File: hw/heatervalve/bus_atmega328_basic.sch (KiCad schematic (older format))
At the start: 26 parts, among them J3 CONN-ISP-6, J4 WAGO 243-723, J5 WAGO 243-724, J6 WAGO 243-721, J7 WAGO 243-722, U1 25LC256, U2 ATMEGA328-TQFP32, U3 7,3728MHz, U4 MAX487ECSA, U5 AM1S-2405

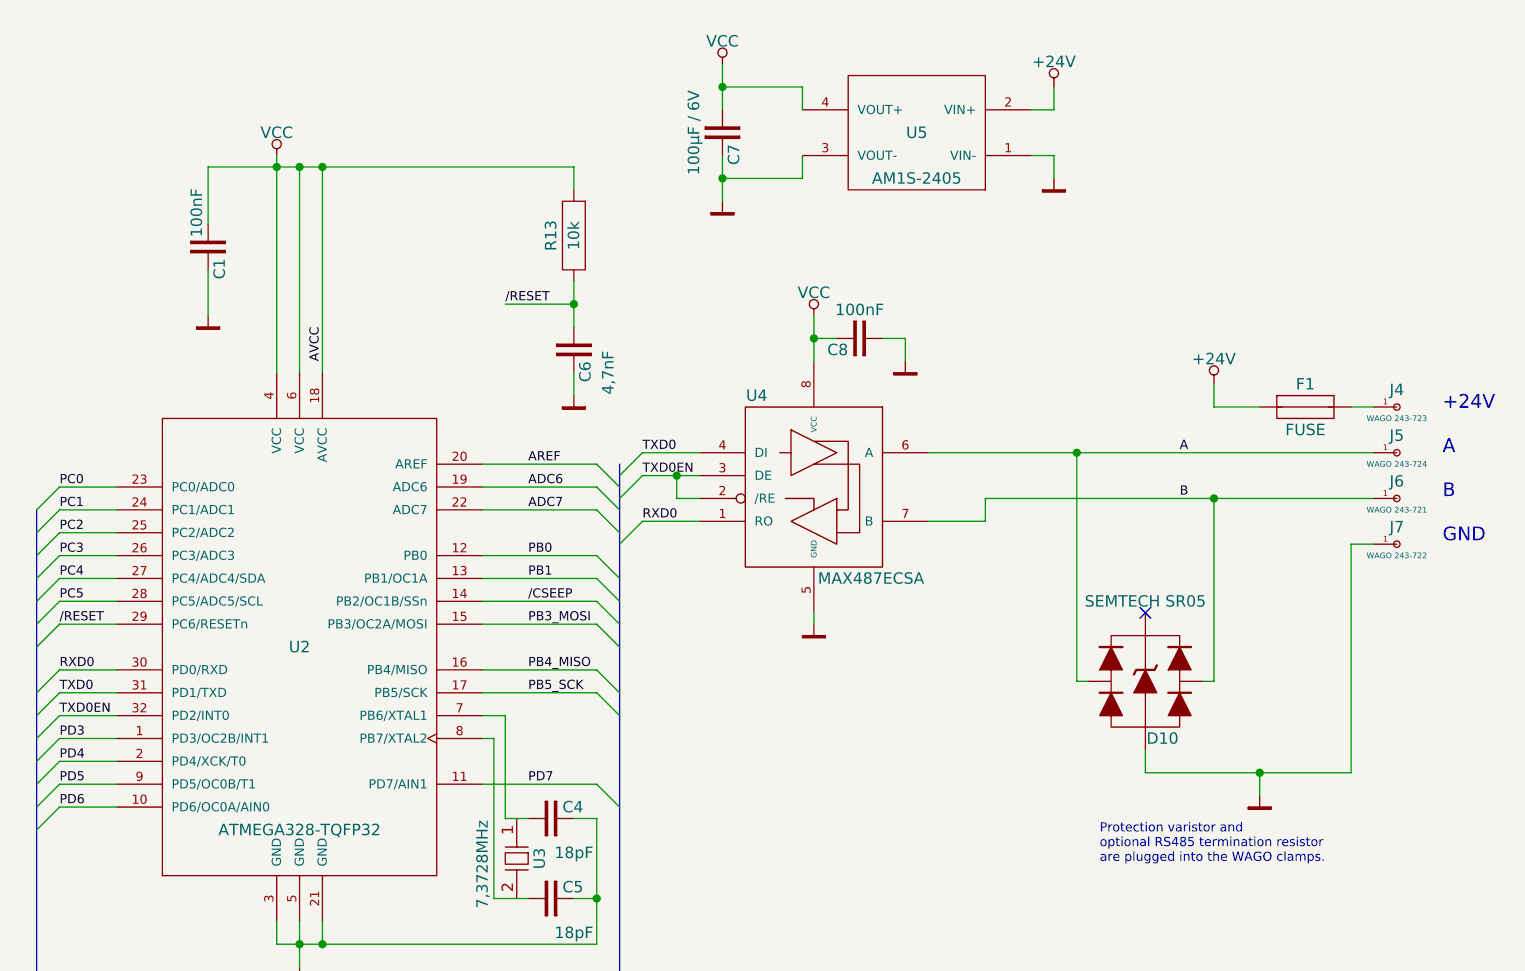
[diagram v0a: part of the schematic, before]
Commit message: first complete draft of heatervalve schematic
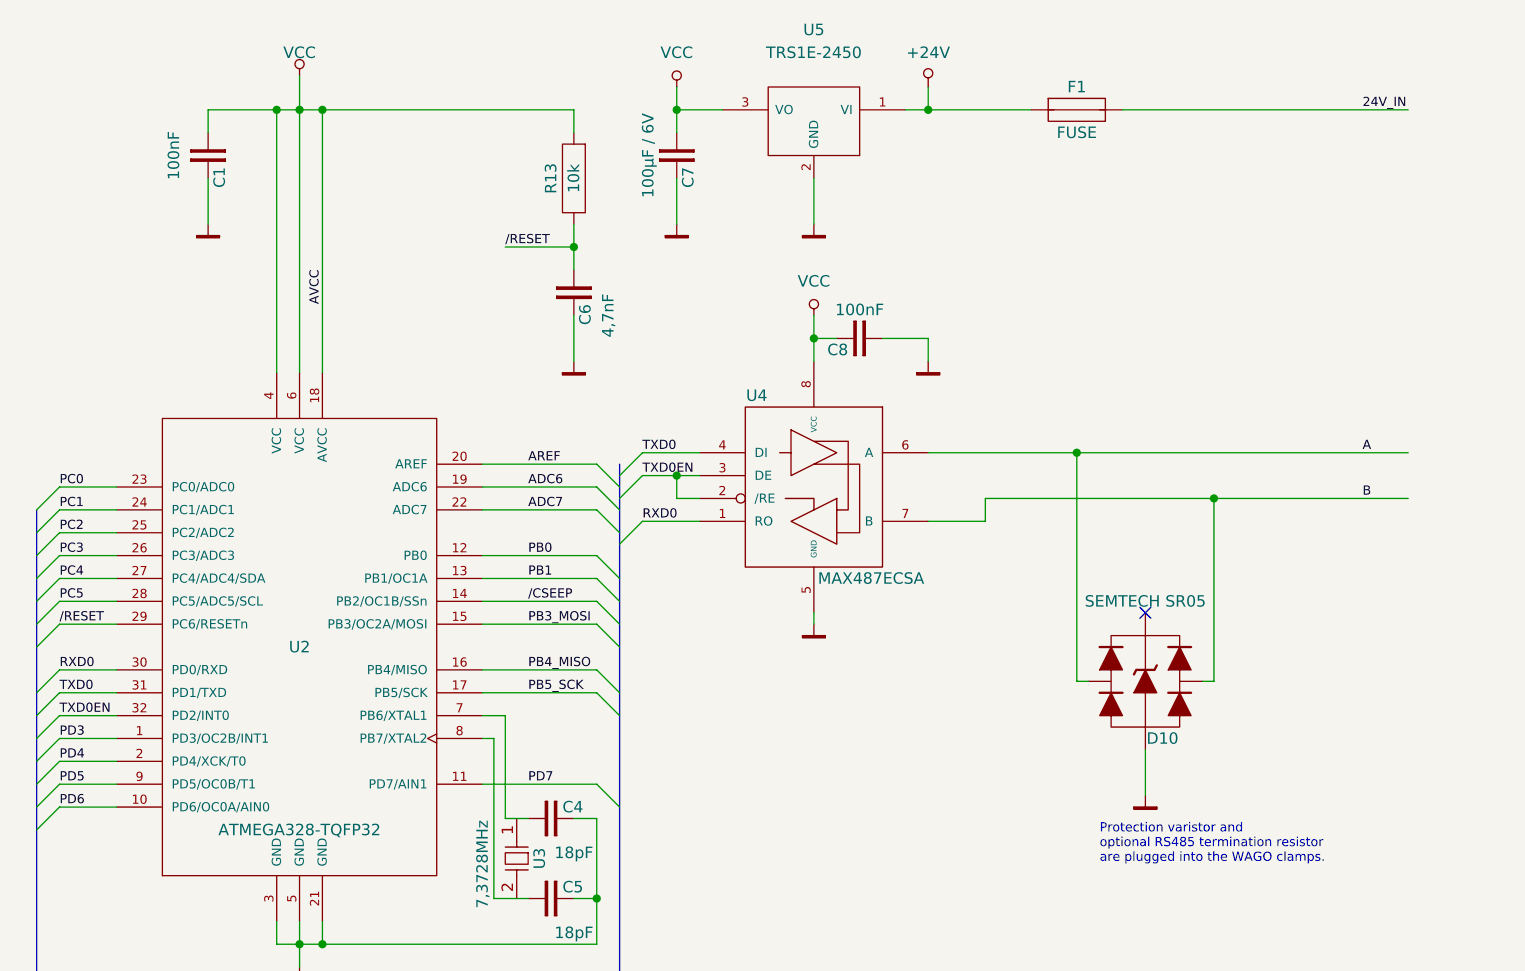
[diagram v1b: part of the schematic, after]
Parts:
- removed J4: WAGO 243-723, Connector_WAGO:WAGO_243, symbol connectors:CONN_1
- removed J5: WAGO 243-724, Connector_WAGO:WAGO_243, symbol connectors:CONN_1
- removed J6: WAGO 243-721, Connector_WAGO:WAGO_243, symbol connectors:CONN_1
- removed J7: WAGO 243-722, Connector_WAGO:WAGO_243, symbol connectors:CONN_1
- removed U5: AM1S-2405, DCDC_Converter:AM1S-XXXX_SIL4, symbol ics_regulator:AM1S-2405
- added U5: TRS1E-2450, DCDC_Converter:TRS1E_SIL3, symbol ics_regulator:TRS1E-2450
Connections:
- net +24V: now also U5.1 (VI)
- net GND: now also U5.2 (GND)
- net VCC: now also U5.3 (VO)
- net 24V_IN: now reaches F1.2
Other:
- note removed: "+24V\n\nA\n\nB \n\nGND"
- moved on the sheet: C1, C6, C7, F1, R13

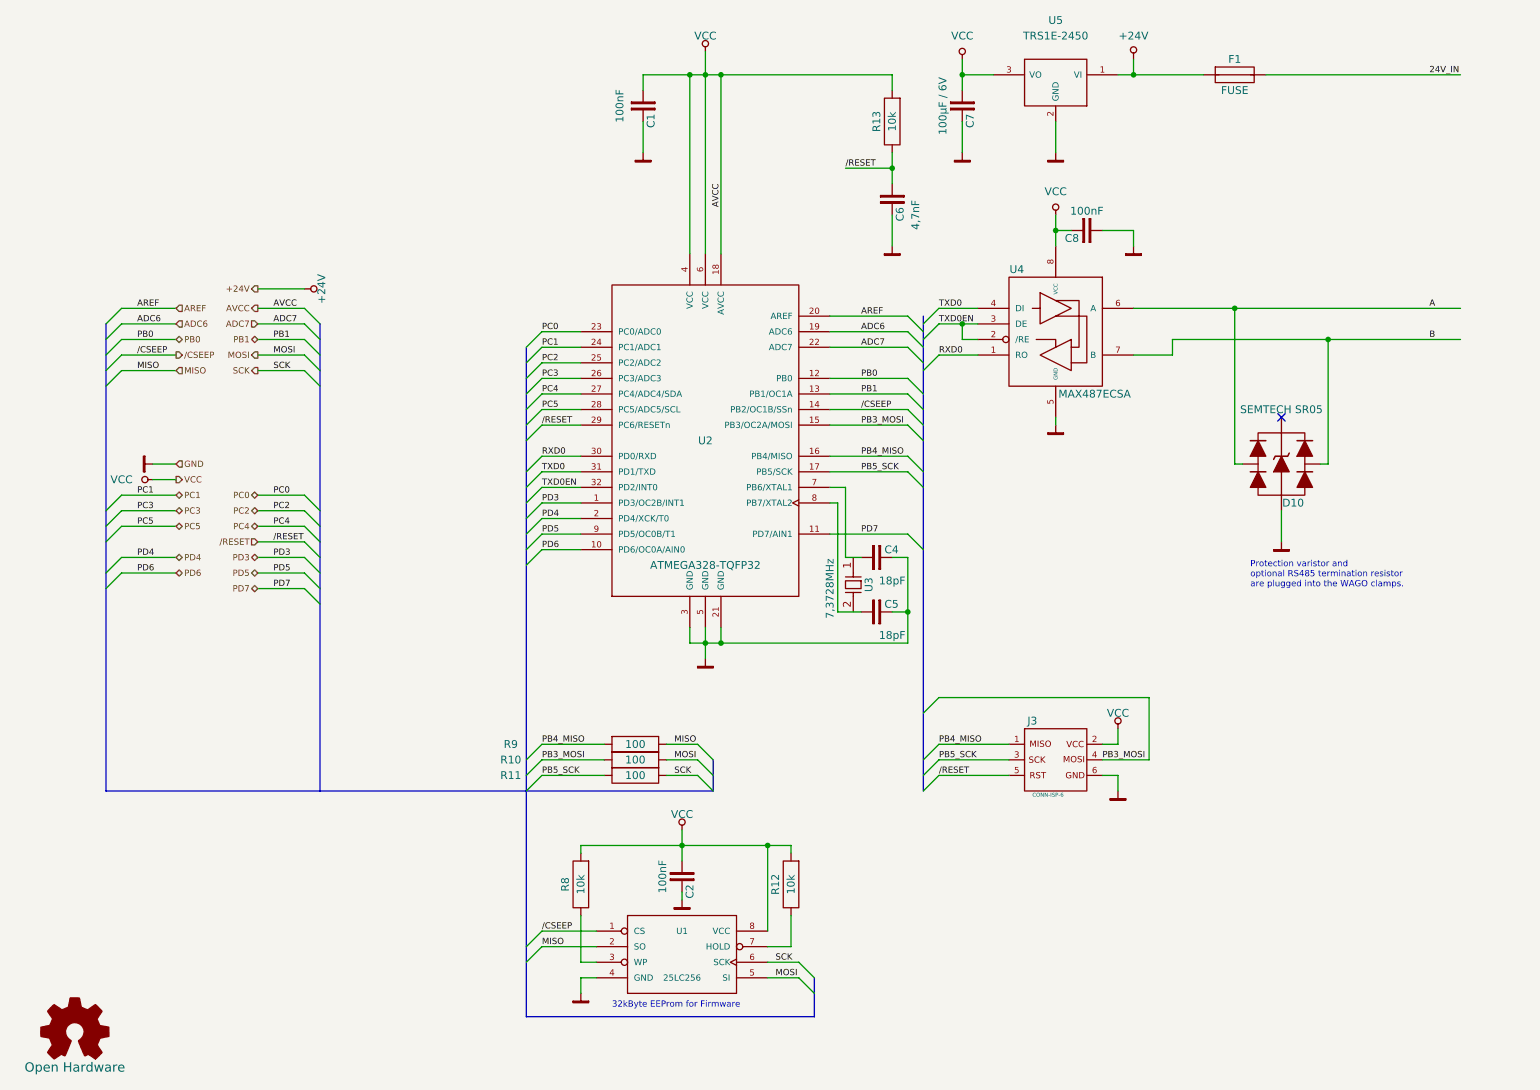
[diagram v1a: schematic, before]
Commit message: Add heatervalve schematic
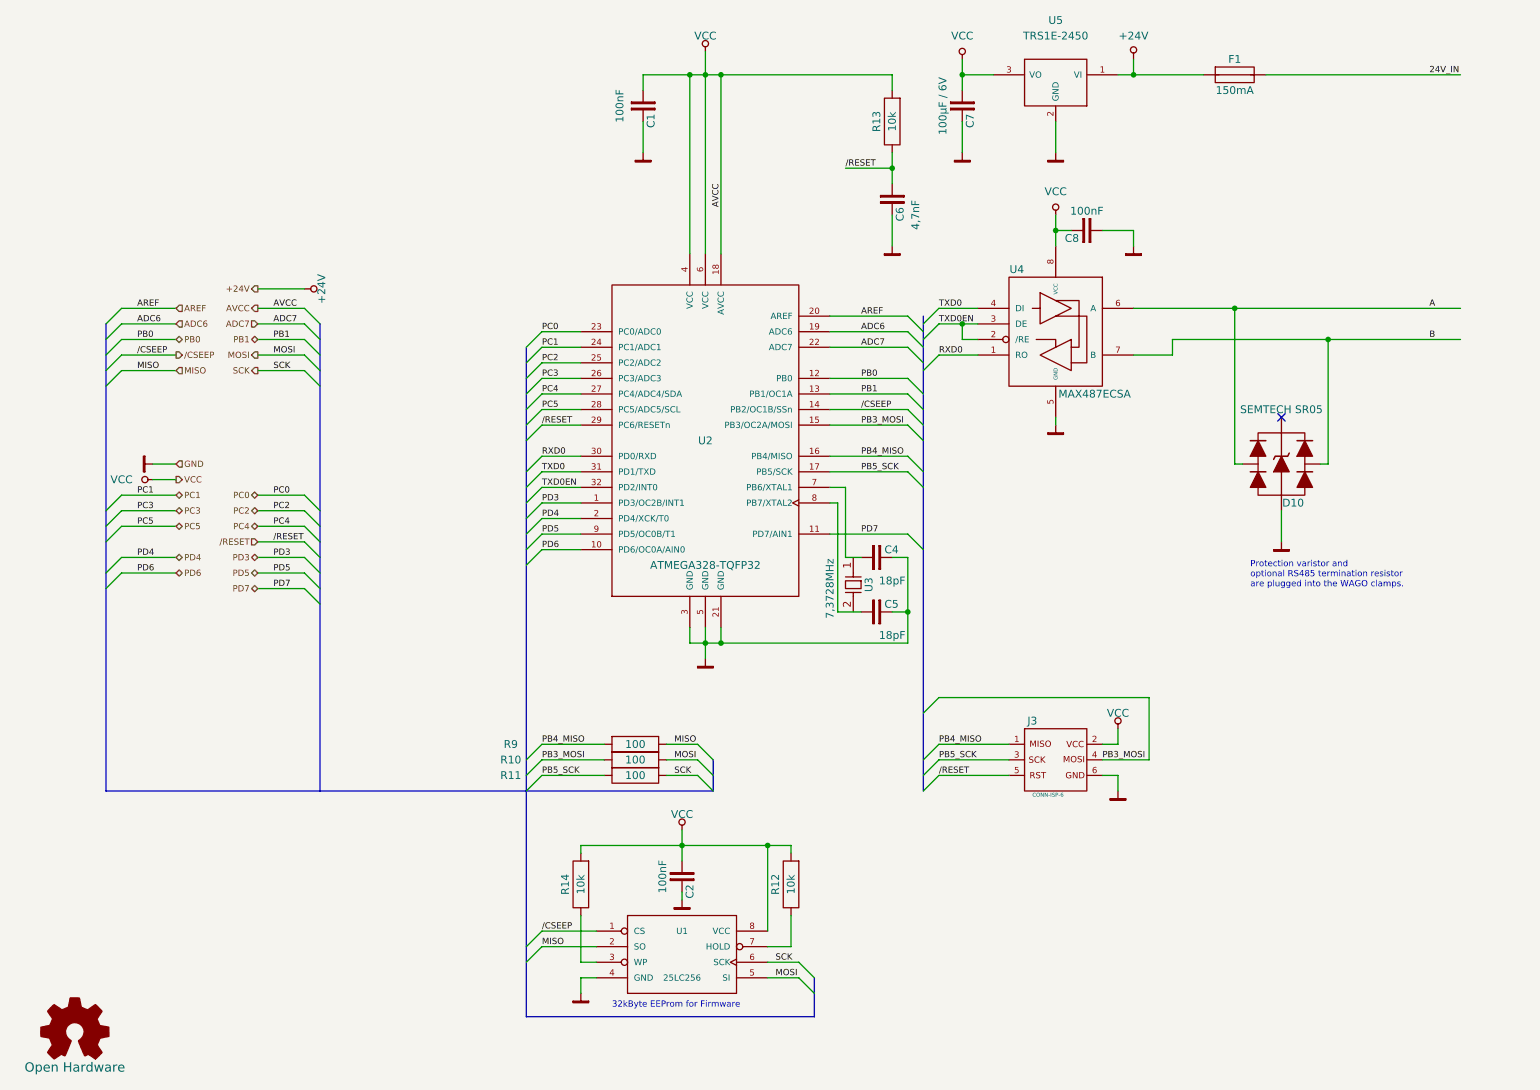
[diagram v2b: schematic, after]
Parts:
- F1: value FUSE -> 150mA
- renumbered R8 to R14
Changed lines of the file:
@@
 SCK
 $Comp
-L standard:R R8
+L standard:R R14
 U 1 1 55A05C69
 P 4550 6400
-F 0 "R8" H 4550 6300 50  0000 C CNN
+F 0 "R14" H 4550 6300 50  0000 C CNN
 F 1 "10k" H 4550 6400 50  0000 C CNN
 F 2 "Resistor:R_0805" H 4550 6400 60  0001 C CNN
@@
 AR Path="/61E7F4A8/56648405" Ref="F1"  Part="1"
 F 0 "F1" H 8750 1300 50  0000 C CNN
-F 1 "FUSE" H 8750 1100 50  0000 C CNN
+F 1 "150mA" H 8750 1100 50  0000 C CNN
 F 2 "Resistor:R_1812" H 8750 1200 60  0001 C CNN
 F 3 "" H 8750 1200 60  0000 C CNN
